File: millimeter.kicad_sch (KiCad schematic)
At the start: 1 part

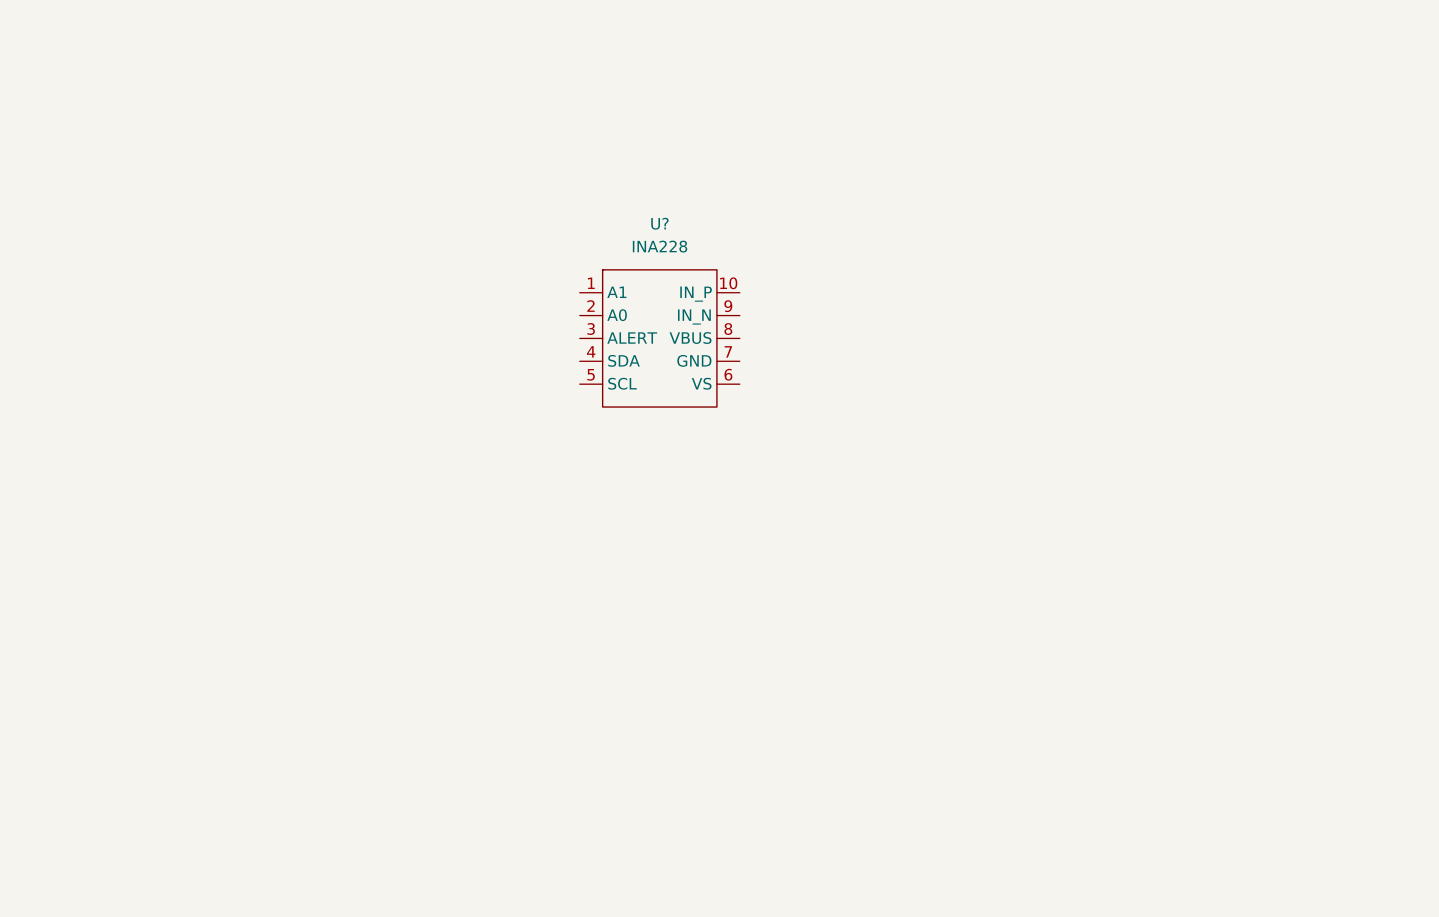
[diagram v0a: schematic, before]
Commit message: Implement Rev 1 schematic
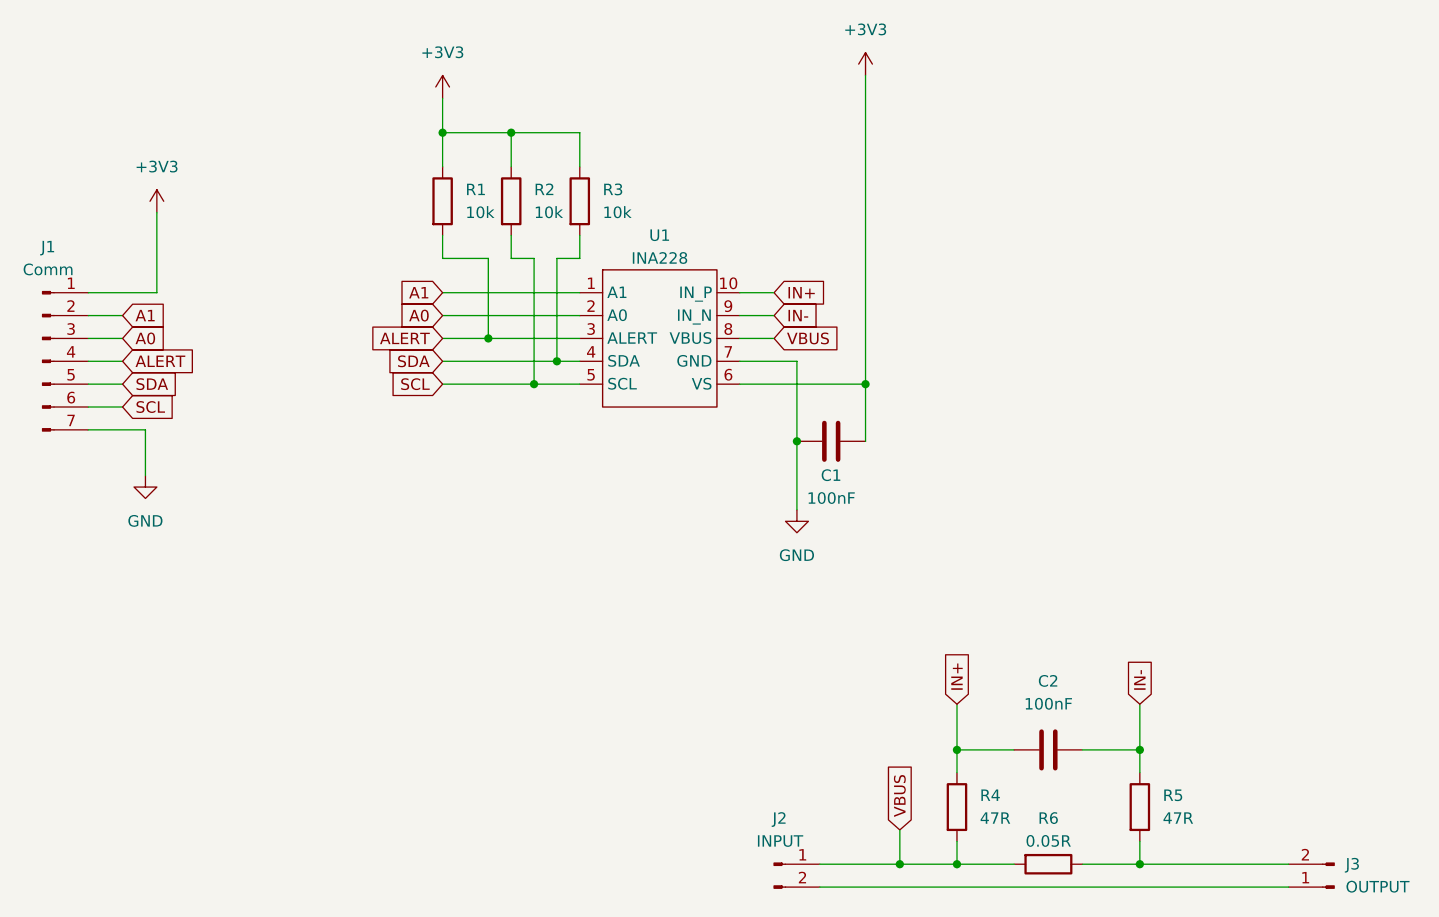
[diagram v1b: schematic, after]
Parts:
- added C1, C2: 100nF, Capacitor_SMD:C_0603_1608Metric_Pad1.08x0.95mm_HandSolder, symbol Device:C
- added J1: Comm, Connector_PinHeader_2.54mm:PinHeader_1x07_P2.54mm_Horizontal, symbol Connector:Conn_01x07_Male
- added J2: INPUT, Connector_PinHeader_2.54mm:PinHeader_1x02_P2.54mm_Vertical, symbol Connector:Conn_01x02_Male
- added J3: OUTPUT, Connector_PinHeader_2.54mm:PinHeader_1x02_P2.54mm_Vertical, symbol Connector:Conn_01x02_Male
- added R1, R2, R3: 10k, Resistor_SMD:R_0603_1608Metric_Pad0.98x0.95mm_HandSolder, symbol Device:R
- added R4, R5: 47R, Resistor_SMD:R_0603_1608Metric_Pad0.98x0.95mm_HandSolder, symbol Device:R
- added R6: 0.05R, Resistor_SMD:R_2512_6332Metric_Pad1.40x3.35mm_HandSolder, symbol Device:R
- U1: renamed from U?; footprint (none) -> Package_SO:VSSOP-10_3x3mm_P0.5mm
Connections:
- net A1: now reaches U1.1 (A1)
- net A1: now also J1.2 (Pin_2)
- net IN+: now reaches U1.10 (IN_P)
- net IN+: now also C2.1, R4.1
- net A0: now reaches U1.2 (A0)
- net A0: now also J1.3 (Pin_3)
- net ALERT: now reaches U1.3 (ALERT)
- net ALERT: now also J1.4 (Pin_4), R1.2
- net SDA: now reaches U1.4 (SDA)
- net SDA: now also J1.5 (Pin_5), R3.2
- net SCL: now reaches U1.5 (SCL)
- net SCL: now also J1.6 (Pin_6), R2.2
- net +3V3: now reaches U1.6 (VS)
- net +3V3: now also C1.2, J1.1 (Pin_1), R1.1, R2.1, R3.1
- net GND: now reaches U1.7 (GND)
- net GND: now also C1.1, J1.7 (Pin_7)
- net VBUS: now reaches U1.8 (VBUS)
- net VBUS: now also J2.1 (Pin_1), R4.2, R6.2
- net IN-: now reaches U1.9 (IN_N)
- net IN-: now also C2.2, R5.1
- new net: J2.2 (Pin_2), J3.1 (Pin_1)
- new net: J3.2 (Pin_2), R5.2, R6.1
